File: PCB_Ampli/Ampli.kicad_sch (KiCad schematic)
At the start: 21 parts

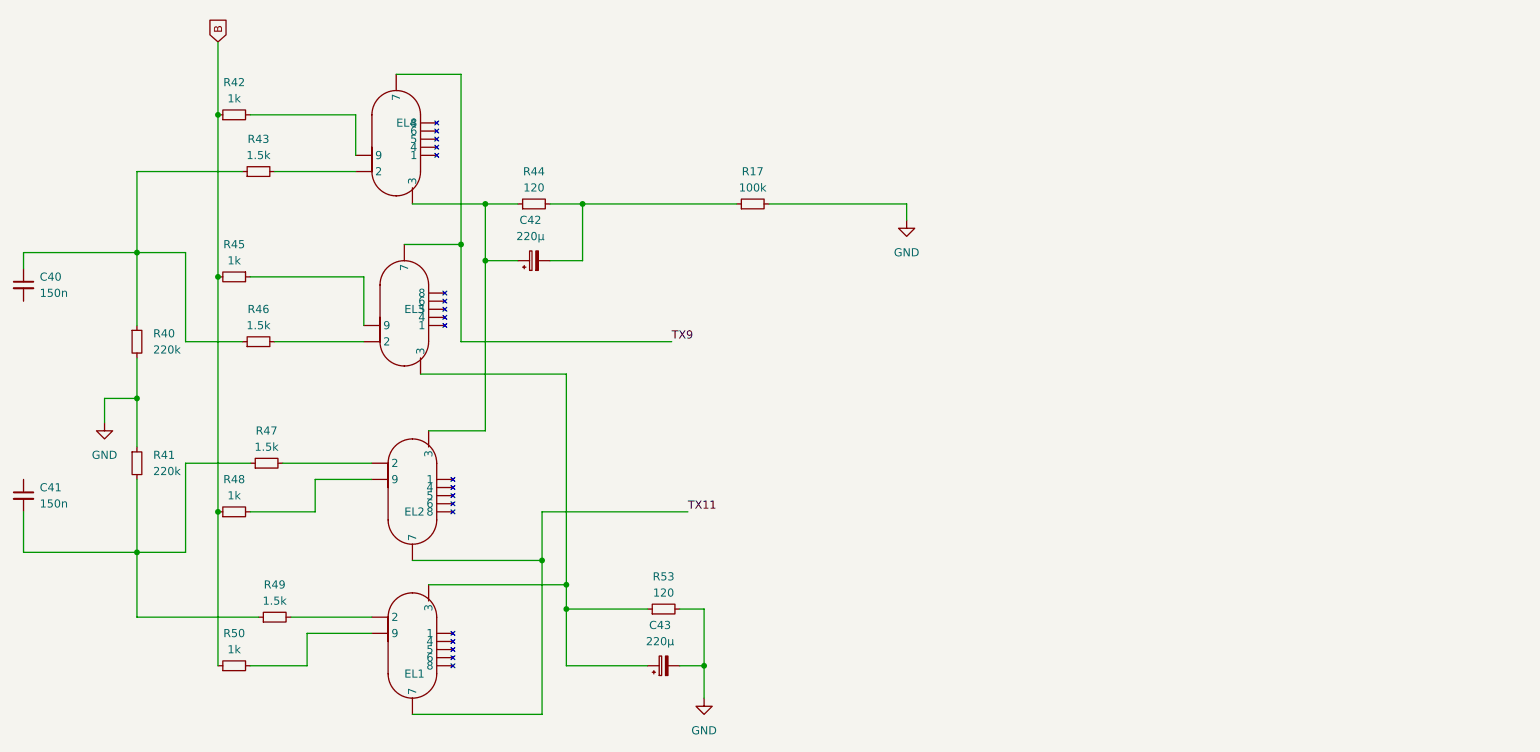
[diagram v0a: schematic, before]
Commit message: PCBV2_Part_Ampli_done
Amplification part using TPA3255 done
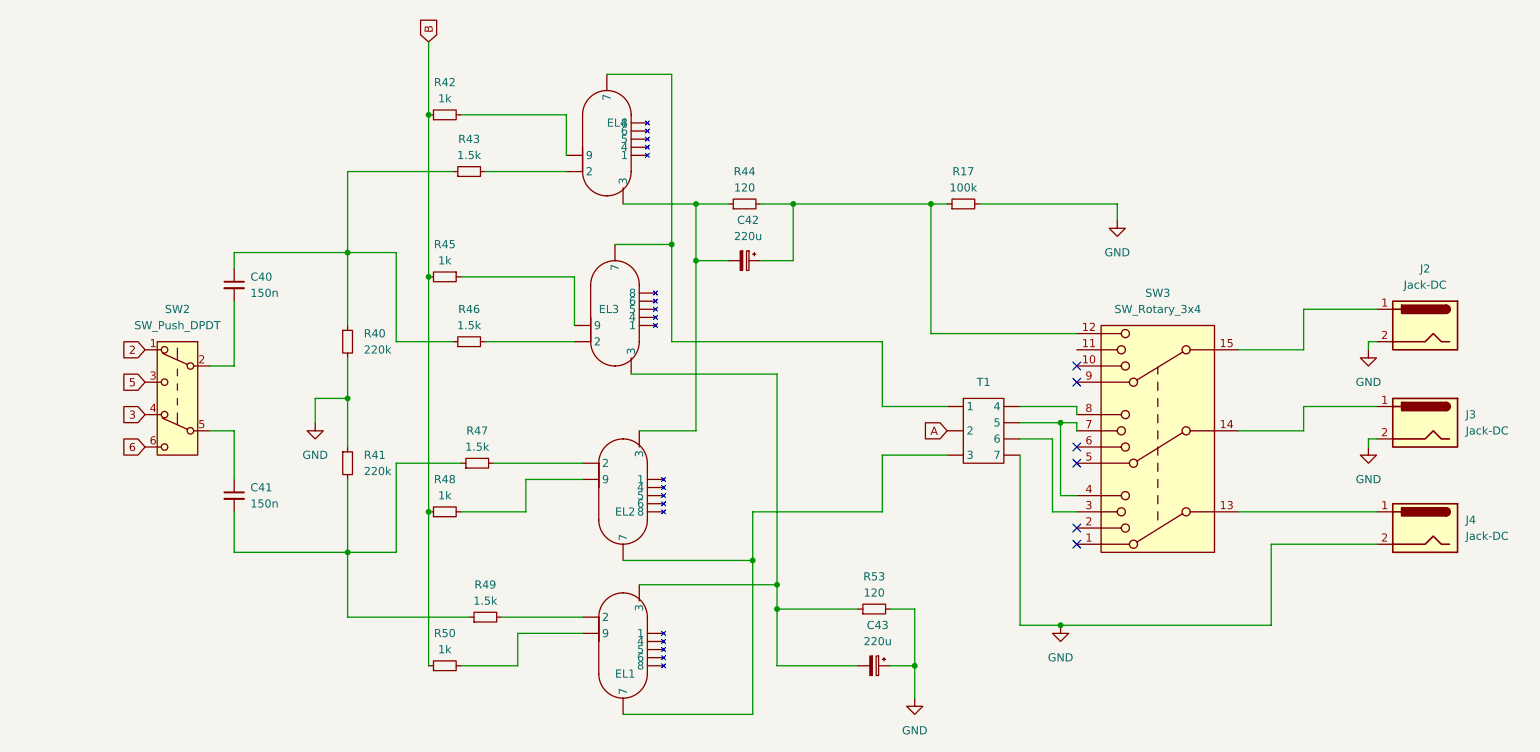
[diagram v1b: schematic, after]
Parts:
- added J2, J3, J4: Jack-DC, symbol Connector:Jack-DC
- added SW2: SW_Push_DPDT, symbol Switch:SW_Push_DPDT
- added SW3: SW_Rotary_3x4, symbol Switch:SW_Rotary_3x4
- added T1: ~, symbol Maker:transfo
- C42, C43: value 220µ -> 220u
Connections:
- net GND: now also C43.1, J2.2, J3.2, J4.2, T1. (7); no longer C43.2
- net at R17.1, R44.2: now also C42.1, SW3.12; no longer C42.2
- net at EL1. (9): now also R50.2
- net at C40.2: now also SW2.2 (B)
- net at EL4. (9): now also R42.2
- net at EL3. (9): now also R45.1
- net at C41.1: now also SW2.5 (B)
- removed net TX11: EL1. (9), EL2. (9)
- removed net TX9: EL3. (9), EL4. (9)
- new net: C42.2, EL2. (9), EL4. (9), R44.1
- new net: C43.2, EL1. (9), EL3. (9), R53.1
- new net: EL1. (9), EL2. (9), T1. (7)
- new net: J4.1, SW3.13
- new net: J3.1, SW3.14
- new net: J2.1, SW3.15
- new net: SW3.3, T1. (7)
- new net: SW3.4, SW3.7, T1. (7)
- new net: SW3.8, T1. (7)
- new net: EL3. (9), EL4. (9), T1. (7)
- new net 2: SW2.1 (A)
- new net 3: SW2.4 (A)
- new net 5: SW2.3 (C)
- new net 6: SW2.6 (C)
- new net A: T1. (7)
- now unconnected: EL2. (9)
- no-connect marks 0 -> 6
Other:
- moved on the sheet: C40, C41, C42, C43, EL1, EL2, EL3, EL4, R17, R40, R41, R42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
